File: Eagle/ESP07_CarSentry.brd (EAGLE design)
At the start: 21.6 x 27.7 mm, 43 parts, among them Q1 PFET, Q2 NPN/NFET, Q3 NPN/NFET, Q4 NPN

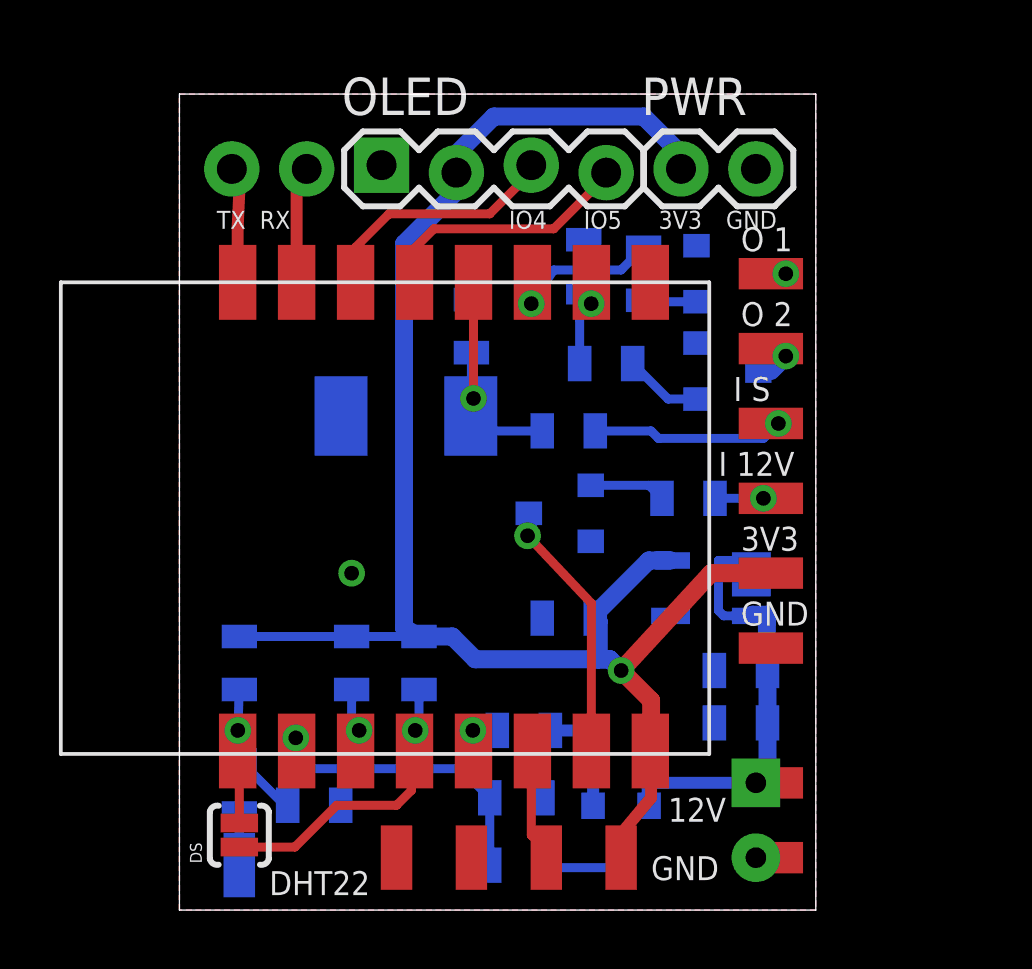
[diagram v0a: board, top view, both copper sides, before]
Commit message: Switched Out 2 to PFET
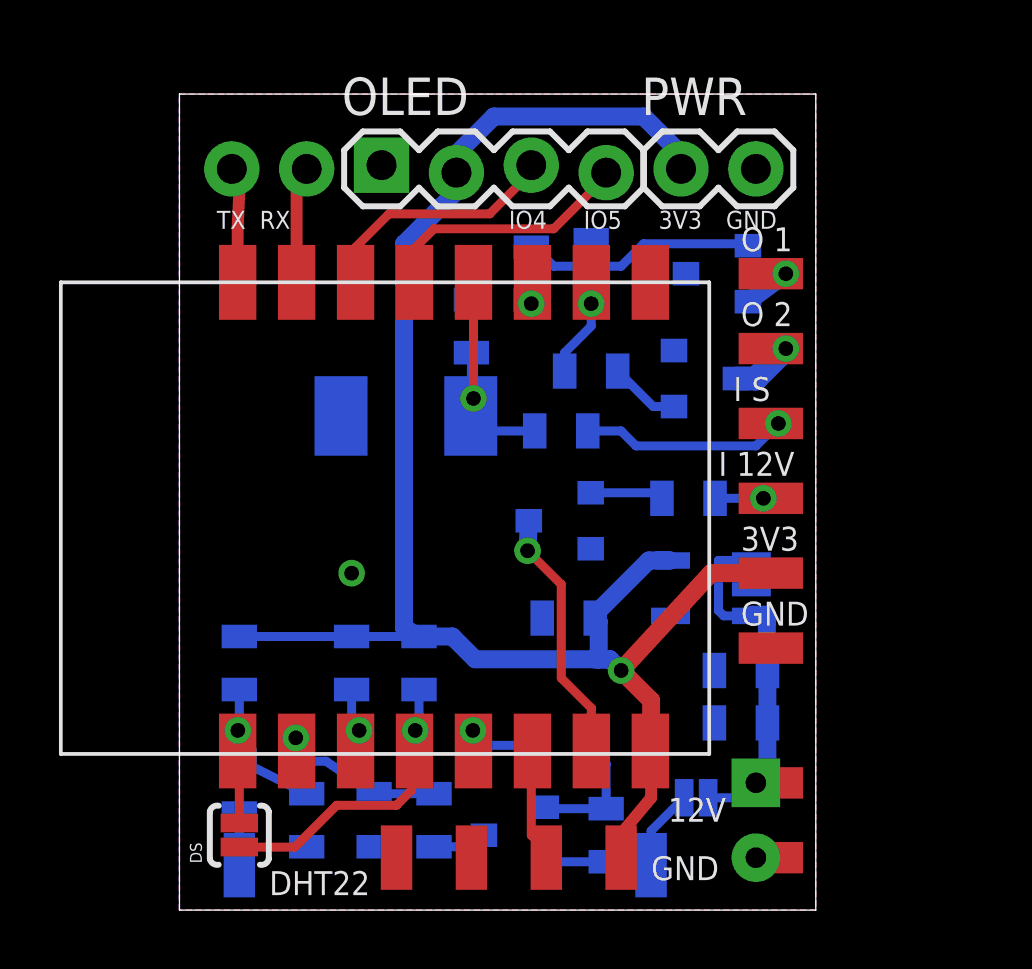
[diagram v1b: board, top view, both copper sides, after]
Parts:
- added 12VA: JUMPER, SparkFun-Passives:PAD-JUMPER-2-NC_BY_PASTE_YES_SILK
- added U$13: SMD-PAD1, CuriousTech:SMD-PAD1
- Q2: value NPN/NFET -> NPN or N-FET
- Q3: value NPN/NFET -> PFET
- moved R11 4.89 mm to (6.60, 3.05), turned to 270 degrees
- moved R6 3.81 mm to (11.9, 21.6), turned to 90 degrees
- moved Q2 3.64 mm to (17.8, 18.0)
- moved Q1 3.56 mm to (11.4, 2.54), turned to 270 degrees
- moved Q3 3.31 mm to (18.3, 21.6), turned to 270 degrees
- moved R10 3.18 mm to (8.64, 3.05), turned to 270 degrees
- moved R5 3.09 mm to (14.5, 2.54), turned to 270 degrees
- moved C5 1.37 mm to (13.0, 5.59)
- moved C8 0.57 mm to (4.32, 3.05), turned to 270 degrees
- moved R9 0.57 mm to (14.0, 18.3)
- moved R1 0.25 mm to (14.0, 21.8)
- moved Q4 0.25 mm to (13.0, 13.2)
- moved R7 0.25 mm to (13.0, 16.3)
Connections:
- new net ADCHI: 12VA.1, Q1.2, R5.2, U$13.>NAME
- net 12V: now also 12VA.2; no longer Q1.2, R5.2
- net GND: now also Q3.3; no longer Q3.2
- net N$2: now also Q3.1; no longer Q2.1
- net N$4: now also Q3.2; no longer Q2.3
- net N$6: now also Q2.1; no longer Q3.1
- net N$7: now also Q2.3; no longer Q3.3
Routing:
- net ADCHI: track 0.00 -> 6.46 mm
- net N$2: track 1.84 -> 7.96 mm
- net ADC: track 10.8 -> 6.32 mm
- net IO2: track 5.48 -> 1.12 mm
- net 12V: track 16.7 -> 12.8 mm
- net IO14: track 1.57 -> 3.05 mm
- net N$7: track 1.71 -> 2.62 mm
- net N$3: track 3.76 -> 4.67 mm
- net N$1: track 2.69 -> 1.92 mm
- net N$4: track 1.44 -> 2.11 mm

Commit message: rev 2 or something
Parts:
- removed C2: (no value), SparkFun-Capacitors:CPOL-RADIAL-100UF-25V
- removed C3: 0.1uF, SparkFun-Capacitors:0805-CAP
- removed PWR: (no value), SparkFun-Connectors:1X02
- removed VREG: MCP1755T-330I/OT, Microchip_By_element14_Batch_1:SOT95P270X145-5N
- added C11, C6, C9: 0.1uF, SparkFun-Capacitors:0805-CAP
- added D5: BAT20J, SparkFun-DiscreteSemi:SOD-323
- added L1, L2: (no value), SparkFun-Passives:0805
- added Q5: NPN, SparkFun-DiscreteSemi:SOT23-3
- added Q6: PFET, SparkFun-DiscreteSemi:SOT23-3
- added R13: 4K7, SparkFun-Resistors:0805
- added R14: 1K, SparkFun-Resistors:0805
- added VREG1: LMR16006YQ3DDCRQ1, CuriousTech:SOT-23-6
- C1: value 0.1uF -> 2.2uF
- C4: value 1uF -> 10uF
- moved C1 14.6 mm to (25.1, 1.52), flipped to the top
- moved U$13 13.5 mm to (25.1, 11.4), turned to 0 degrees
- moved U$10 9.37 mm to (25.1, 19.3), flipped to the bottom
- moved Q4 5.86 mm to (18.8, 12.7)
- moved U$6 5.85 mm to (25.9, 1.52), flipped to the bottom, turned to 270 degrees
- moved U$3 5.80 mm to (25.1, 21.8), flipped to the bottom
- moved U$9 5.80 mm to (25.1, 24.4), flipped to the bottom
- moved Q2 5.76 mm to (22.1, 21.8)
- moved R9 5.14 mm to (18.3, 21.1)
- moved R12 5.09 mm to (22.4, 13.7)
- moved U$11 5.08 mm to (25.1, 8.89), flipped to the bottom
- moved U$14 5.08 mm to (25.1, 16.5), flipped to the bottom
- moved U$2 5.08 mm to (25.1, 14.0), flipped to the bottom
- moved Q3 5.03 mm to (21.8, 25.1)
- moved U$16 4.33 mm to (23.4, 1.52), flipped to the bottom, turned to 270 degrees
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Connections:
- removed net 12V: 12VA.2, C2.1, C3.1, C4.1, U$16.>NAME, VREG.1, VREG.3
- new net +12V: 12VA.2, C1.1, C6.1, U$16.>NAME, VREG1.5
- new net N$12: Q5.1, R13.2
- new net N$13: C11.1, D5.C, L1.1, L2.1, VREG1.6
- new net N$14: C11.2, VREG1.1
- new net N$15: R13.1, U$10.>NAME
- new net N$16: Q6.2, U$13.>NAME
- new net N$17: Q6.1, R14.2
- net 3V3: now also C4.1, C9.1, L1.2, L2.2, VREG1.3; no longer C1.1, PWR.1, U$10.>NAME, VREG.5
- net ADCHI: no longer U$13.>NAME
- net GND: now also C6.2, C9.2, D5.A, Q5.2, Q6.3, VREG1.2; no longer C2.2, C3.2, PWR.2, VREG.2
- net RXD: now also Q5.3
- net TXD: now also R14.1
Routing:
- net TXD: track 3.89 -> 25.5 mm
- net RXD: track 3.93 -> 23.4 mm
- net +12V: track 0.00 -> 15.9 mm, vias 0 -> 1
- net 12V: track 12.8 -> 0.00 mm
- net N$13: track 0.00 -> 12.2 mm
- net 3V3: track 60.1 -> 48.4 mm, vias 1 -> 2
- net N$2: track 7.96 -> 13.7 mm
- net N$5: track 7.25 -> 10.5 mm, vias 1 -> 0
- net N$16: track 0.00 -> 2.72 mm, vias 0 -> 1
- net N$15: track 0.00 -> 2.30 mm, vias 0 -> 1
- net N$14: track 0.00 -> 2.27 mm
- net GND: track 0.00 -> 2.01 mm
- net N$17: track 0.00 -> 1.89 mm
- net ADCHI: track 6.46 -> 4.76 mm
- net N$12: track 0.00 -> 1.65 mm
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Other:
- board size 21.6 x 27.7 mm -> 26.9 x 27.4 mm
- board text removed: "3V3"
